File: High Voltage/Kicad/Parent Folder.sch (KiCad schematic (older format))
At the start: 25 parts

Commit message: Loading characterization & other comments
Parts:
- added Q? (x4): STN0214, teensy:STN0214, symbol STN0214
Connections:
- net GND: now also Q?.1 (E), Q?.1 (E), Q?.1 (E), Q?.1 (E)
- net -12V: now reaches U?.4 (V-)
- net -12V: now also U?.4 (V-), U?.4 (V-), U?.4 (V-)
- net +12V: now reaches U?.8 (V+)
- net +12V: now also U?.8 (V+), U?.8 (V+), U?.8 (V+)
- net at C?.1, R?.1: now also Q?.3 (B) (x3)
- net at R?.1, U?.1: now also Q?.3 (B)
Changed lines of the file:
@@
 	1    0    0    -1
 $EndComp
-Wire Wire Line
-	2900 1500 3000 1500
-Wire Wire Line
-	2950 1550 2950 1500
-Connection ~ 2950 1500
-Wire Wire Line
-	2900 2700 3000 2700
-Wire Wire Line
-	2950 2750 2950 2700
-Connection ~ 2950 2700
-Wire Wire Line
-	2900 3950 3000 3950
-Wire Wire Line
-	2950 4000 2950 3950
-Connection ~ 2950 3950
 $Comp
 L GND #PWR?
@@
 	1    0    0    -1
 $EndComp
-Wire Wire Line
-	2950 1950 2950 2000
-Wire Wire Line
-	2950 4400 2950 4450
-Wire Wire Line
-	2950 3150 2950 3200
 $Comp
 L C C?
@@
 	1    0    0    -1
 $EndComp
-Wire Wire Line
-	3550 3150 3550 3200
 $Comp
 L C C?
@@
 	1    0    0    -1
 $EndComp
-Wire Wire Line
-	3550 1950 3550 2000
 $Comp
 L C C?
@@
 	1    0    0    -1
 $EndComp
-Wire Wire Line
-	3550 4400 3550 4450
-Wire Wire Line
-	3500 1500 3550 1500
-Wire Wire Line
-	3550 1500 3550 1550
-Wire Wire Line
-	3500 2700 3550 2700
-Wire Wire Line
-	3550 2700 3550 2750
-Wire Wire Line
-	3500 3950 3550 3950
-Wire Wire Line
-	3550 3950 3550 4000
 $Comp
 L R R?
@@
 	0    1    1    0
 $EndComp
-Wire Wire Line
-	1650 1600 1650 2100
-Wire Wire Line
-	1650 2100 1750 2100
-Wire Wire Line
-	2250 2100 2350 2100
-Wire Wire Line
-	2350 2100 2350 1500
 $Comp
 L R R?
@@
 	-1   0    0    1
 $EndComp
-Wire Wire Line
-	1500 1600 1650 1600
 $Comp
 L R R?
@@
 	0    1    1    0
 $EndComp
-Wire Wire Line
-	1650 2800 1650 3300
-Wire Wire Line
-	1650 3300 1750 3300
-Wire Wire Line
-	2250 3300 2350 3300
-Wire Wire Line
-	2350 3300 2350 2700
 $Comp
 L R R?
@@
 	-1   0    0    1
 $EndComp
-Wire Wire Line
-	1500 2800 1650 2800
 $Comp
 L OP275 U?
@@
 	0    1    1    0
 $EndComp
-Wire Wire Line
-	1650 4050 1650 4550
-Wire Wire Line
-	1650 4550 1750 4550
-Wire Wire Line
-	2250 4550 2350 4550
-Wire Wire Line
-	2350 4550 2350 3950
 $Comp
 L R R?
@@
 	-1   0    0    1
 $EndComp
-Wire Wire Line
-	1500 4050 1650 4050
 $Comp
 L OP275 U?
@@
 	0    1    1    0
 $EndComp
-Wire Wire Line
-	1700 5300 1700 5800
-Wire Wire Line
-	1700 5800 1800 5800
-Wire Wire Line
-	2300 5800 2400 5800
-Wire Wire Line
-	2400 5800 2400 5200
 $Comp
 L R R?
@@
 	-1   0    0    1
 $EndComp
-Wire Wire Line
-	1550 5300 1700 5300
-Wire Wire Line
-	2350 1500 2400 1500
-Wire Wire Line
-	2350 2700 2400 2700
-Wire Wire Line
-	2350 3950 2400 3950
 $Comp
 L GND #PWR?
@@
 	1    0    0    -1
 $EndComp
-Wire Wire Line
-	1500 3300 1500 3350
-Wire Wire Line
-	1500 4550 1500 4600
 $Comp
 L GND #PWR?
@@
 	1    0    0    -1
 $EndComp
+$Comp
+L STN0214 Q?
+U 1 1 54F334D3
+P 3800 1500
+F 0 "Q?" H 3800 1351 40  0000 R CNN
+F 1 "STN0214" H 3700 1650 40  0000 R CNN
+F 2 "teensy:STN0214" H 3575 1600 29  0000 C CNN
+F 3 "" H 3800 1500 60  0000 C CNN
+	1    3800 1500
+	1    0    0    -1
+$EndComp
+$Comp
+L STN0214 Q?
+U 1 1 54F3354C
+P 3800 2700
+F 0 "Q?" H 3800 2551 40  0000 R CNN
+F 1 "STN0214" H 3700 2850 40  0000 R CNN
+F 2 "teensy:STN0214" H 3575 2800 29  0000 C CNN
+F 3 "" H 3800 2700 60  0000 C CNN
+	1    3800 2700
+	1    0    0    -1
+$EndComp
+$Comp
+L STN0214 Q?
+U 1 1 54F33607
+P 3800 3950
+F 0 "Q?" H 3800 3801 40  0000 R CNN
+F 1 "STN0214" H 3700 4100 40  0000 R CNN
+F 2 "teensy:STN0214" H 3575 4050 29  0000 C CNN
+F 3 "" H 3800 3950 60  0000 C CNN
+	1    3800 3950
+	1    0    0    -1
+$EndComp
+$Comp
+L STN0214 Q?
+U 1 1 54F336C8
+P 2650 5200
+F 0 "Q?" H 2650 5051 40  0000 R CNN
+F 1 "STN0214" H 2550 5350 40  0000 R CNN
+F 2 "teensy:STN0214" H 2425 5300 29  0000 C CNN
+F 3 "" H 2650 5200 60  0000 C CNN
+	1    2650 5200
+	1    0    0    -1
+$EndComp
+$Comp
+L GND #PWR?
+U 1 1 54F33797
+P 3900 4200
+F 0 "#PWR?" H 3900 3950 60  0001 C CNN
+F 1 "GND" H 3900 4050 60  0000 C CNN
+F 2 "" H 3900 4200 60  0000 C CNN
+F 3 "" H 3900 4200 60  0000 C CNN
+	1    3900 4200
+	1    0    0    -1
+$EndComp
+$Comp
+L GND #PWR?
+U 1 1 54F3381F
+P 3900 2950
+F 0 "#PWR?" H 3900 2700 60  0001 C CNN
+F 1 "GND" H 3900 2800 60  0000 C CNN
+F 2 "" H 3900 2950 60  0000 C CNN
+F 3 "" H 3900 2950 60  0000 C CNN
+	1    3900 2950
+	1    0    0    -1
+$EndComp
+$Comp
+L GND #PWR?
+U 1 1 54F338E1
+P 3900 1750
+F 0 "#PWR?" H 3900 1500 60  0001 C CNN
+F 1 "GND" H 3900 1600 60  0000 C CNN
+F 2 "" H 3900 1750 60  0000 C CNN
+F 3 "" H 3900 1750 60  0000 C CNN
+	1    3900 1750
+	1    0    0    -1
+$EndComp
+$Comp
+L GND #PWR?
+U 1 1 54F33A34
+P 2750 5450
+F 0 "#PWR?" H 2750 5200 60  0001 C CNN
+F 1 "GND" H 2750 5300 60  0000 C CNN
+F 2 "" H 2750 5450 60  0000 C CNN
+F 3 "" H 2750 5450 60  0000 C CNN
+	1    2750 5450
+	1    0    0    -1
+$EndComp
+Wire Wire Line
+	2900 1500 3000 1500
+Wire Wire Line
+	2950 1550 2950 1500
+Connection ~ 2950 1500
+Wire Wire Line
+	2900 2700 3000 2700
+Wire Wire Line
+	2950 2750 2950 2700
+Connection ~ 2950 2700
+Wire Wire Line
+	2900 3950 3000 3950
+Wire Wire Line
+	2950 4000 2950 3950
+Connection ~ 2950 3950
+Wire Wire Line
+	2950 1950 2950 2000
+Wire Wire Line
+	2950 4400 2950 4450
+Wire Wire Line
+	2950 3150 2950 3200
+Wire Wire Line
+	3550 3150 3550 3200
+Wire Wire Line
+	3550 1950 3550 2000
+Wire Wire Line
+	3550 4400 3550 4450
+Wire Wire Line
+	3500 1500 3600 1500
+Wire Wire Line
+	3550 1500 3550 1550
+Wire Wire Line
+	3500 2700 3600 2700
+Wire Wire Line
+	3550 2700 3550 2750
+Wire Wire Line
+	3500 3950 3600 3950
+Wire Wire Line
+	3550 3950 3550 4000
+Wire Wire Line
+	1650 1600 1650 2100
+Wire Wire Line
+	1650 2100 1750 2100
+Wire Wire Line
+	2250 2100 2350 2100
+Wire Wire Line
+	2350 2100 2350 1500
+Wire Wire Line
+	1500 1600 1650 1600
+Wire Wire Line
+	1650 2800 1650 3300
+Wire Wire Line
+	1650 3300 1750 3300
+Wire Wire Line
+	2250 3300 2350 3300
+Wire Wire Line
+	2350 3300 2350 2700
+Wire Wire Line
+	1500 2800 1650 2800
+Wire Wire Line
+	1650 4050 1650 4550
+Wire Wire Line
+	1650 4550 1750 4550
+Wire Wire Line
+	2250 4550 2350 4550
+Wire Wire Line
+	2350 4550 2350 3950
+Wire Wire Line
+	1500 4050 1650 4050
+Wire Wire Line
+	1700 5300 1700 5800
+Wire Wire Line
+	1700 5800 1800 5800
+Wire Wire Line
+	2300 5800 2400 5800
+Wire Wire Line
+	2400 5800 2400 5200
+Wire Wire Line
+	1550 5300 1700 5300
+Wire Wire Line
+	2350 1500 2400 1500
+Wire Wire Line
+	2350 2700 2400 2700
+Wire Wire Line
+	2350 3950 2400 3950
+Wire Wire Line
+	1500 3300 1500 3350
+Wire Wire Line
+	1500 4550 1500 4600
 Wire Wire Line
 	1550 5850 1550 5800
+Wire Wire Line
+	2750 5400 2750 5450
+Wire Wire Line
+	3900 4200 3900 4150
+Wire Wire Line
+	2400 5200 2450 5200
+Connection ~ 3550 3950
+Connection ~ 3550 2700
+Wire Wire Line
+	3900 2900 3900 2950
+Wire Wire Line
+	3900 1700 3900 1750
+Connection ~ 3550 1500
+$Comp
+L +12V #PWR?
+U 1 1 54F4C6A5
+P 1950 4900
+F 0 "#PWR?" H 1950 4750 60  0001 C CNN
+F 1 "+12V" H 1950 5040 60  0000 C CNN
+F 2 "" H 1950 4900 60  0000 C CNN
+F 3 "" H 1950 4900 60  0000 C CNN
+	1    1950 4900
+	1    0    0    -1
+$EndComp
+$Comp
+L +12V #PWR?
+U 1 1 54F4CCF4
+P 1900 3650
+F 0 "#PWR?" H 1900 3500 60  0001 C CNN
+F 1 "+12V" H 1900 3790 60  0000 C CNN
+F 2 "" H 1900 3650 60  0000 C CNN
+F 3 "" H 1900 3650 60  0000 C CNN
+	1    1900 3650
+	1    0    0    -1
+$EndComp
+$Comp
+L +12V #PWR?
+U 1 1 54F4CD08
+P 1900 2400
+F 0 "#PWR?" H 1900 2250 60  0001 C CNN
+F 1 "+12V" H 1900 2540 60  0000 C CNN
+F 2 "" H 1900 2400 60  0000 C CNN
+F 3 "" H 1900 2400 60  0000 C CNN
+	1    1900 2400
+	1    0    0    -1
+$EndComp
+$Comp
+L +12V #PWR?
+U 1 1 54F4CD56
+P 1900 1200
+F 0 "#PWR?" H 1900 1050 60  0001 C CNN
+F 1 "+12V" H 1900 1340 60  0000 C CNN
+F 2 "" H 1900 1200 60  0000 C CNN
+F 3 "" H 1900 1200 60  0000 C CNN
+	1    1900 1200
+	1    0    0    -1
+$EndComp
+$Comp
+L -12V #PWR?
+U 1 1 54F4CDA4
+P 1900 1800
+F 0 "#PWR?" H 1900 1900 20  0001 C CNN
+F 1 "-12V" H 1900 1950 60  0000 C CNN
+F 2 "" H 1900 1800 60  0000 C CNN
+F 3 "" H 1900 1800 60  0000 C CNN
+	1    1900 1800
+	-1   0    0    1
+$EndComp
+$Comp
+L -12V #PWR?
+U 1 1 54F4CE58
+P 1900 3000
+F 0 "#PWR?" H 1900 3100 20  0001 C CNN
+F 1 "-12V" H 1900 3150 60  0000 C CNN
+F 2 "" H 1900 3000 60  0000 C CNN
+F 3 "" H 1900 3000 60  0000 C CNN
+	1    1900 3000
+	-1   0    0    1
+$EndComp
+$Comp
+L -12V #PWR?
+U 1 1 54F4CEE0
+P 1900 4250
+F 0 "#PWR?" H 1900 4350 20  0001 C CNN
+F 1 "-12V" H 1900 4400 60  0000 C CNN
+F 2 "" H 1900 4250 60  0000 C CNN
+F 3 "" H 1900 4250 60  0000 C CNN
+	1    1900 4250
+	-1   0    0    1
+$EndComp
+$Comp
+L -12V #PWR?
+U 1 1 54F4CF68
+P 1950 5500
+F 0 "#PWR?" H 1950 5600 20  0001 C CNN
+F 1 "-12V" H 1950 5650 60  0000 C CNN
+F 2 "" H 1950 5500 60  0000 C CNN
+F 3 "" H 1950 5500 60  0000 C CNN
+	1    1950 5500
+	-1   0    0    1
+$EndComp
 $EndSCHEMATC

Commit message: PWM1
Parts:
- added TP? (x5): Test_point, symbol Test_point
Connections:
- net at R?.1, R?.2, U?.7: now also TP?.1
- net at R?.1, R?.2, U?.1: now also TP?.1
- net at Q?.3 (B), R?.1, U?.1: now also TP?.1
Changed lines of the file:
@@
 	-1   0    0    1
 $EndComp
+$Comp
+L Test_point TP?
+U 1 1 54FE0871
+P 2300 900
+F 0 "TP?" H 2300 1150 49  0000 C CNN
+F 1 "Test_point" H 2300 1250 49  0001 C CNN
+F 2 "" H 2300 900 49  0000 C CNN
+F 3 "" H 2300 900 49  0000 C CNN
+	1    2300 900
+	1    0    0    -1
+$EndComp
+$Comp
+L Test_point TP?
+U 1 1 54FE1798
+P 2400 2700
+F 0 "TP?" H 2400 2950 49  0000 C CNN
+F 1 "Test_point" H 2400 3050 49  0001 C CNN
+F 2 "" H 2400 2700 49  0000 C CNN
+F 3 "" H 2400 2700 49  0000 C CNN
+	1    2400 2700
+	1    0    0    -1
+$EndComp
+$Comp
+L Test_point TP?
+U 1 1 54FE17D0
+P 2400 1475
+F 0 "TP?" H 2400 1725 49  0000 C CNN
+F 1 "Test_point" H 2400 1825 49  0001 C CNN
+F 2 "" H 2400 1475 49  0000 C CNN
+F 3 "" H 2400 1475 49  0000 C CNN
+	1    2400 1475
+	1    0    0    -1
+$EndComp
+$Comp
+L Test_point TP?
+U 1 1 54FE33BF
+P 2400 3950
+F 0 "TP?" H 2400 4200 49  0000 C CNN
+F 1 "Test_point" H 2400 4300 49  0001 C CNN
+F 2 "" H 2400 3950 49  0000 C CNN
+F 3 "" H 2400 3950 49  0000 C CNN
+	1    2400 3950
+	1    0    0    -1
+$EndComp
+$Comp
+L Test_point TP?
+U 1 1 54FE5643
+P 2450 5200
+F 0 "TP?" H 2450 5450 49  0000 C CNN
+F 1 "Test_point" H 2450 5550 49  0001 C CNN
+F 2 "" H 2450 5200 49  0000 C CNN
+F 3 "" H 2450 5200 49  0000 C CNN
+	1    2450 5200
+	1    0    0    -1
+$EndComp
 $EndSCHEMATC

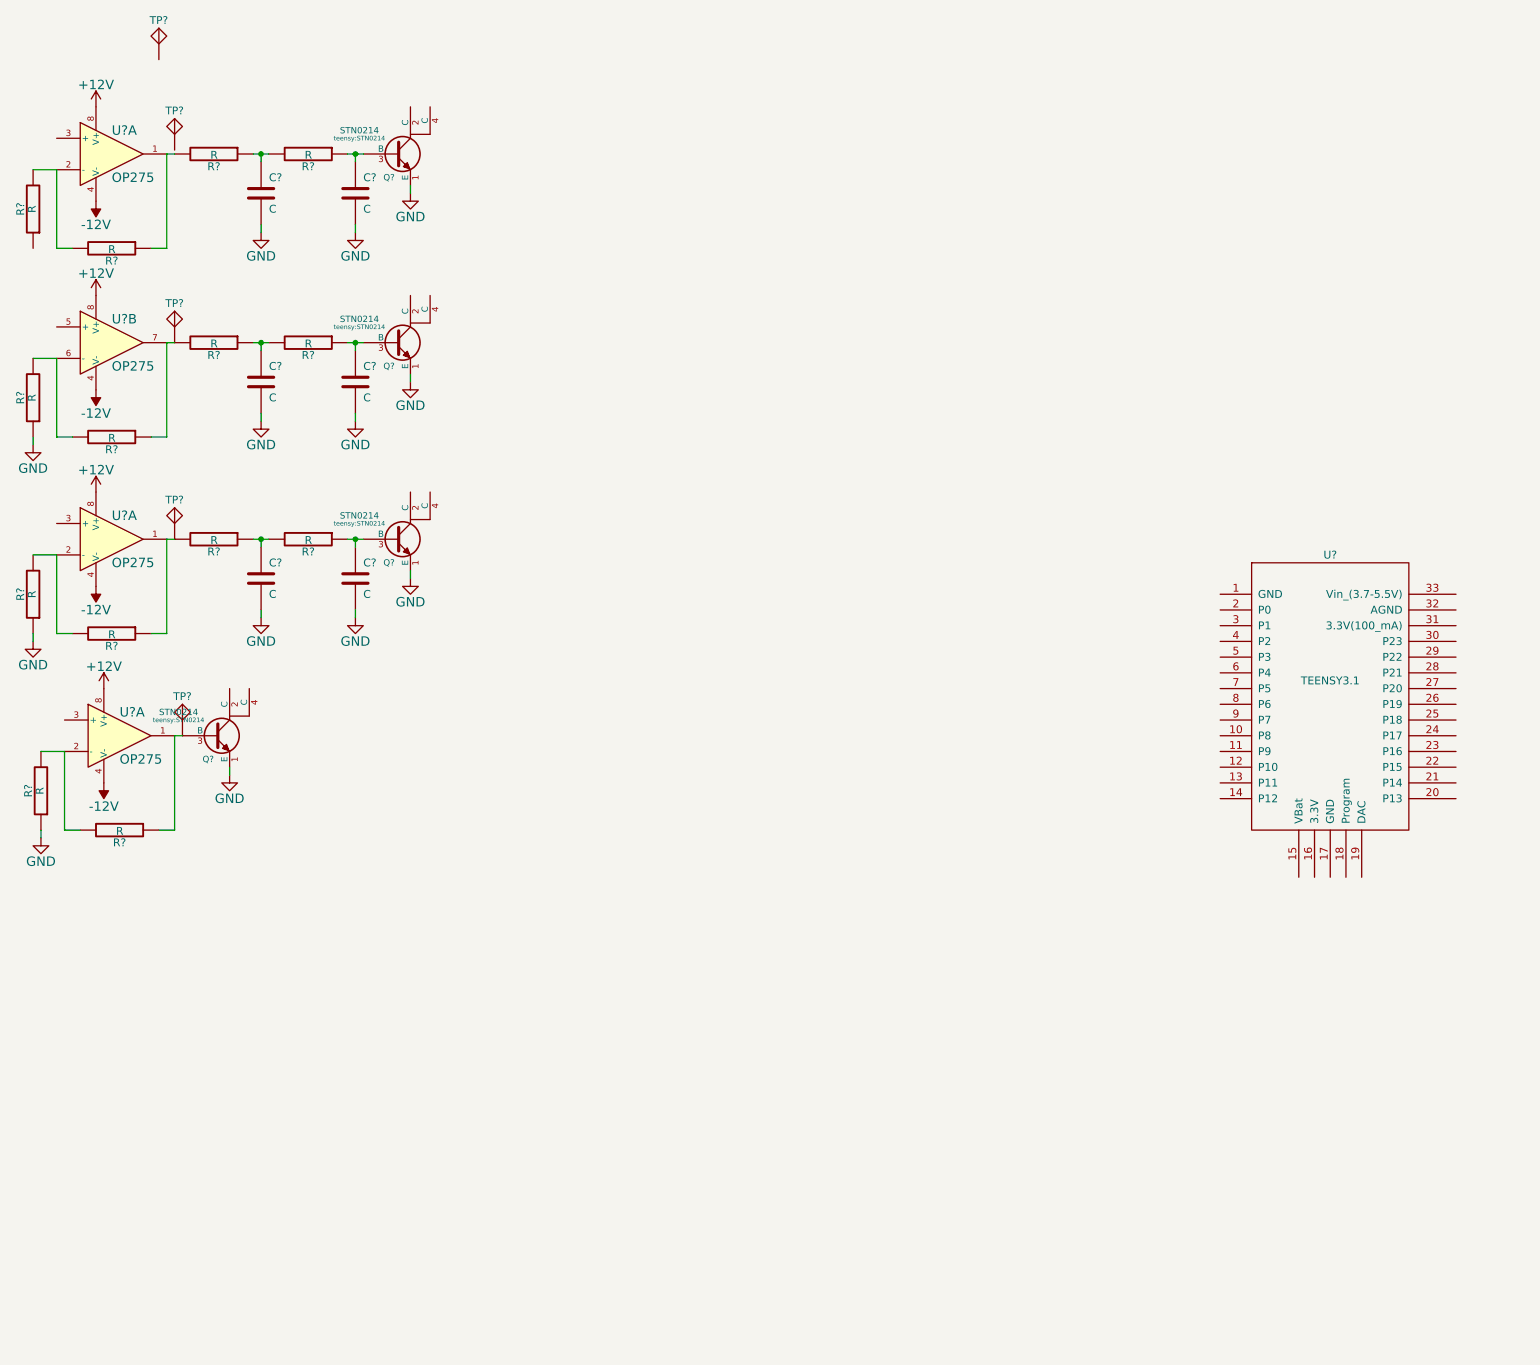
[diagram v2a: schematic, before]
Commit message: High voltage schematic changes
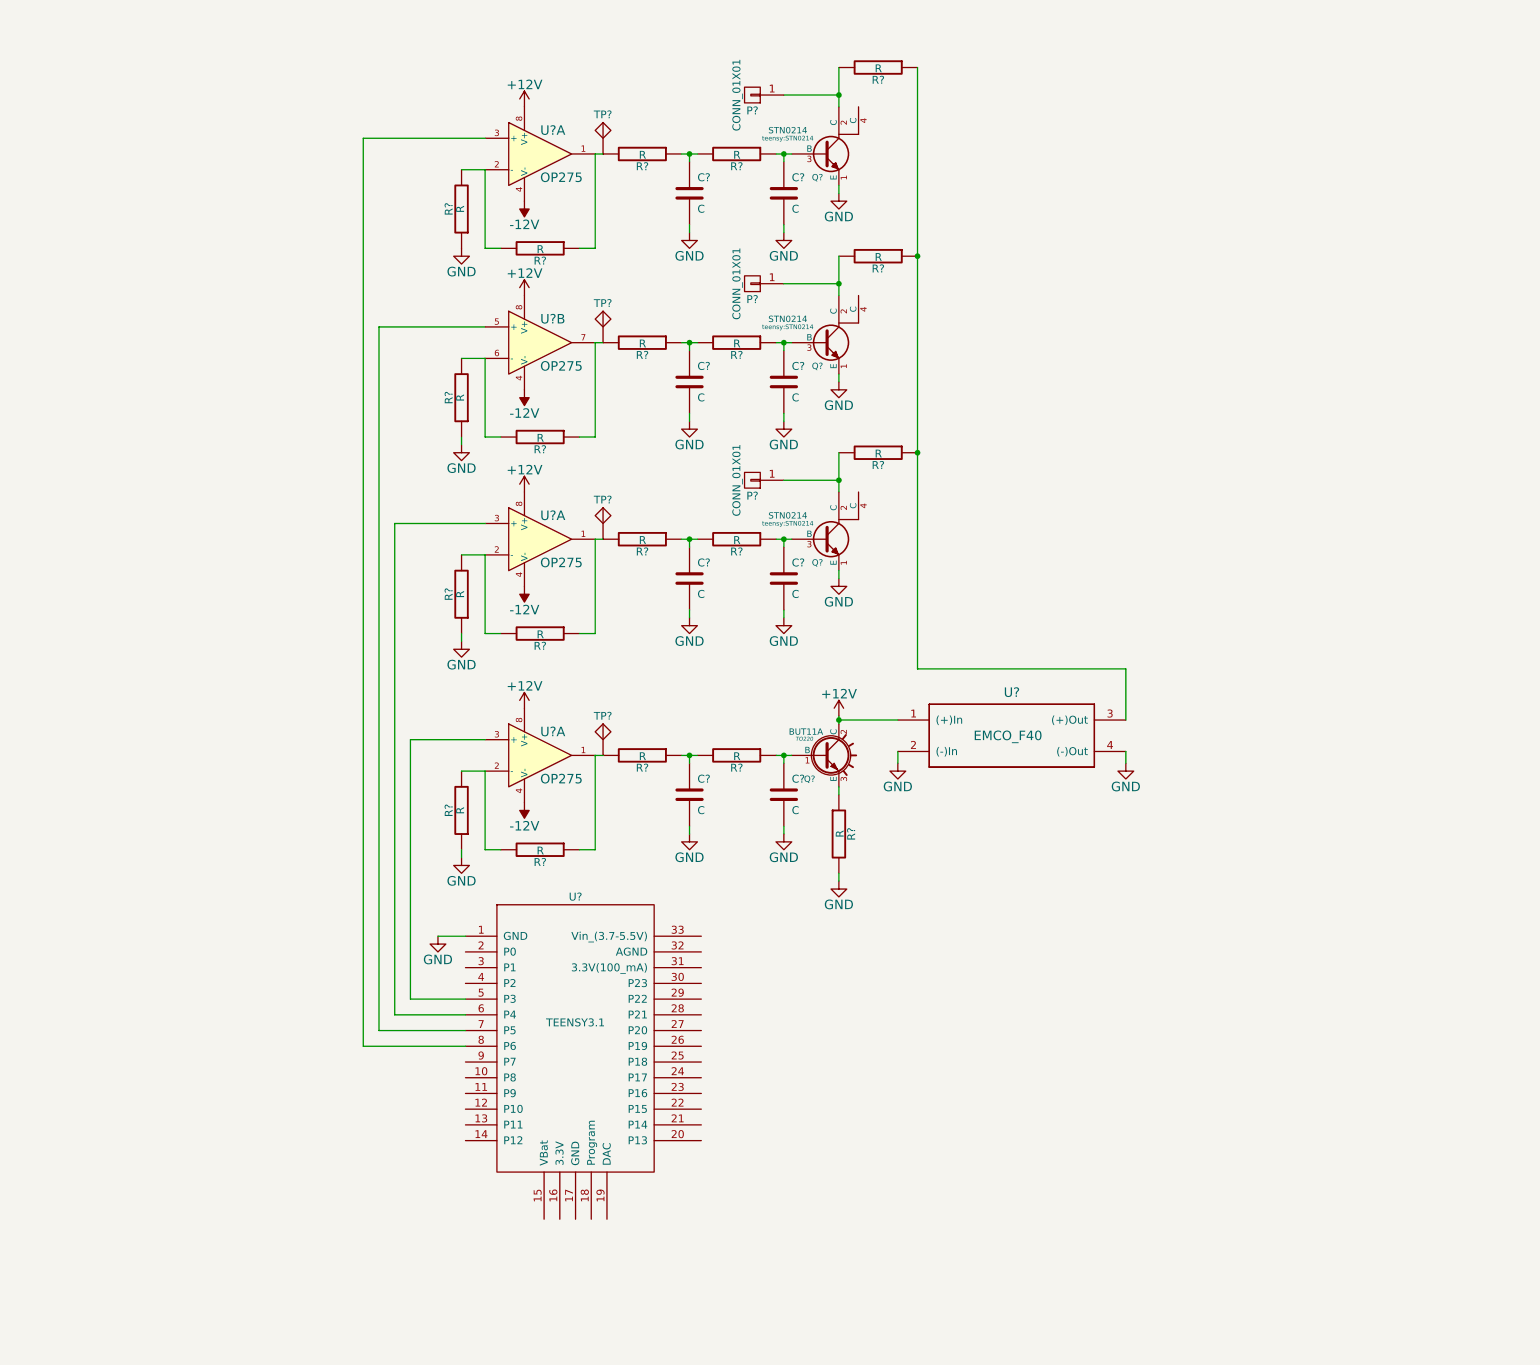
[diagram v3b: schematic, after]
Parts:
- removed Q?: STN0214, teensy:STN0214, symbol STN0214
- removed TP?: Test_point, symbol Test_point
- added C? (x2): C, symbol C
- added P? (x3): CONN_01X01, symbol CONN_01X01
- added Q?: BUT11A, TO220, symbol BUT11A
- added R? (x6): R, symbol R
- added U?: EMCO_F40, symbol EMCO_F40
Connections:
- net +12V: now also Q?.2 (C), U?.1 ((+)In)
- net GND: now also R?.1, U?.1 (GND), C?.2, C?.2, R?.2, U?.2 ((-)In), U?.4 ((-)Out)
- net at U?.5 (P3): now also U?.3 (+)
- net at U?.6 (P4): now also U?.3 (+)
- net at U?.7 (P5): now also U?.5 (+)
- net at U?.8 (P6): now also U?.3 (+)
- net at R?.1, R?.2, U?.1: now also TP?.1
- net at R?.1, TP?.1, U?.1: now also R?.2
- net at Q?.2 (C): now also P?.1 (P1), R?.2 (x3)
- new net: C?.1, Q?.1 (B), R?.1
- new net: Q?.3 (E), R?.1
- new net: C?.1, R?.1, R?.2
- new net: R?.1, R?.1, R?.1, U?.3 ((+)Out)
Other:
- moved on the sheet: C?, Q?, R?, TP?, U?, U?A, U?B
